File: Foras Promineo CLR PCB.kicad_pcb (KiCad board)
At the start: 2 copper layers, 40 x 40 mm, 21 parts, among them J1 Conn_01x10_Male

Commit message: FM DONE!
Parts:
- D3: footprint Foras_Promineo:1212_LED_Pol_End -> Foras_Promineo_Github_Local:1212_LED_Pol
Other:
- board text added: "FORAS PROMINEO LED RING - CLR REV: FLIGHT NB, CK 06/2022"
- board text removed: "CLR FORAS PROMINEO LED RING REV: FLIGHT NB, CK 4/2022 SN:"
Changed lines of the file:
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@@
   (setup
     (stackup
-      (layer "F.SilkS" (type "Top Silk Screen"))
+      (layer "F.SilkS" (type "Top Silk Screen") (color "Black"))
       (layer "F.Paste" (type "Top Solder Paste"))
-      (layer "F.Mask" (type "Top Solder Mask") (thickness 0.01))
+      (layer "F.Mask" (type "Top Solder Mask") (color "White") (thickness 0.01))
       (layer "F.Cu" (type "copper") (thickness 0.035))
       (layer "dielectric 1" (type "core") (thickness 1.51) (material "FR4") (epsilon_r 4.5) (loss_tangent 0.02))
       (layer "B.Cu" (type "copper") (thickness 0.035))
-      (layer "B.Mask" (type "Bottom Solder Mask") (thickness 0.01))
+      (layer "B.Mask" (type "Bottom Solder Mask") (color "White") (thickness 0.01))
       (layer "B.Paste" (type "Bottom Solder Paste"))
-      (layer "B.SilkS" (type "Bottom Silk Screen"))
+      (layer "B.SilkS" (type "Bottom Silk Screen") (color "Black"))
       (copper_finish "None")
       (dielectric_constraints no)
@@
     (grid_origin 80 88)
     (pcbplotparams
-      (layerselection 0x00010fc_ffffffff)
+      (layerselection 0x00210ff_ffffffff)
       (disableapertmacros false)
       (usegerberextensions true)
@@
       (drillshape 0)
       (scaleselection 1)
-      (outputdirectory "../../../Foras Promineo CLR PCB/")
+      (outputdirectory "Fab Files/")
     )
   )
@@
     )
   )
-  (footprint "Foras_Promineo:1212_LED_Pol_End" (layer "F.Cu")
+  (footprint "Foras_Promineo_Github_Local:1212_LED_Pol" (layer "F.Cu")
     (at 89.289 96.684 45)
     (property "Description" "LED Lighting series White - 2.75V 65mA 120° 1212 (3030 Metric)")
@@
     (property "Supplier Part Number" "1510-SPMWHD32AMH1XAH0S0CT-ND")
     (attr through_hole)
-    (fp_text reference "D3" (at -0.286378 2.706098 45) (layer "F.SilkS")
+    (fp_text reference "D3" (at 3.956262 -0.122329 45) (layer "F.SilkS")
       (effects (font (size 1 1) (thickness 0.15)))
     )
@@
       (effects (font (size 1 1) (thickness 0.15)))
     )
-    (fp_circle (center 1.25 2.5) (end 1.5 2.5) (layer "F.SilkS") (width 0.15) (fill solid))
-    (fp_line (start -1.3 -1.6) (end 1.3 -1.6) (layer "Eco1.User") (width 0.12))
-    (fp_line (start -1.3 1.6) (end -1.3 -1.6) (layer "Eco1.User") (width 0.12))
+    (fp_line (start 2.5 -1.75) (end 2.5 1.75) (layer "F.SilkS") (width 0.15))
     (fp_line (start 1.3 1.6) (end -1.3 1.6) (layer "Eco1.User") (width 0.12))
     (fp_line (start 1.3 -1.6) (end 1.3 1.6) (layer "Eco1.User") (width 0.12))
+    (fp_line (start -1.3 -1.6) (end 1.3 -1.6) (layer "Eco1.User") (width 0.12))
+    (fp_line (start -1.3 1.6) (end -1.3 -1.6) (layer "Eco1.User") (width 0.12))
     (pad "1" smd rect (at 1.025 0 45) (size 1.75 3.5) (layers "F.Cu" "F.Paste" "F.Mask")
       (net 12 "/LED_3") (pinfunction "K") (pintype "passive"))
@@
     (property "Supplier Part Number" "1510-SPMWHD32AMH1XAH0S0CT-ND")
     (attr through_hole)
-    (fp_text reference "D4" (at 1.640488 -3.112684 225) (layer "F.SilkS")
+    (fp_text reference "D4" (at 3.478965 0.140007 225) (layer "F.SilkS")
       (effects (font (size 1 1) (thickness 0.15)))
     )
@@
   (gr_line (start 98 60) (end 62 60) (layer "Edge.Cuts") (width 0.1))
   (gr_arc (start 98 60) (mid 99.414214 60.585786) (end 100 62) (layer "Edge.Cuts") (width 0.1))
-  (gr_text "CLR\nFORAS PROMINEO LED RING\nREV: FLIGHT\nNB, CK\n4/2022\nSN:" (at 79.9 63.5) (layer "F.SilkS")
+  (gr_text "FORAS PROMINEO LED RING - CLR\nREV: FLIGHT\nNB, CK\n06/2022" (at 79.8 63.2) (layer "F.SilkS")
     (effects (font (size 0.75 0.75) (thickness 0.15)))
   )

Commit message: FM
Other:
- board text added: "FORAS PROMINEO LED RING - CLR REV: FM NB, CK 09/2022"
- board text removed: "FORAS PROMINEO LED RING - CLR REV: FLIGHT NB, CK 06/2022"
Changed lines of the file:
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@@
       (drillshape 0)
       (scaleselection 1)
-      (outputdirectory "Fab Files/")
+      (outputdirectory "Fab Files/FM/")
     )
   )
@@
     )
   )
+  (gr_rect (start 91.380005 71.390002) (end 98.009989 98.349994) (layer "B.SilkS") (width 0.254) (fill none))
   (gr_circle (center 94.73 66.55) (end 96.73 66.55) (layer "Eco1.User") (width 0.2) (fill none))
   (gr_circle (center 65.27 66.55) (end 67.27 66.55) (layer "Eco1.User") (width 0.2) (fill none))
@@
   (gr_line (start 98 60) (end 62 60) (layer "Edge.Cuts") (width 0.1))
   (gr_arc (start 98 60) (mid 99.414214 60.585786) (end 100 62) (layer "Edge.Cuts") (width 0.1))
-  (gr_text "FORAS PROMINEO LED RING - CLR\nREV: FLIGHT\nNB, CK\n06/2022" (at 79.8 63.2) (layer "F.SilkS")
+  (gr_text "FORAS PROMINEO LED RING - CLR\nREV: FM\nNB, CK\n09/2022" (at 79.799993 63.200001) (layer "F.SilkS")
     (effects (font (size 0.75 0.75) (thickness 0.15)))
   )

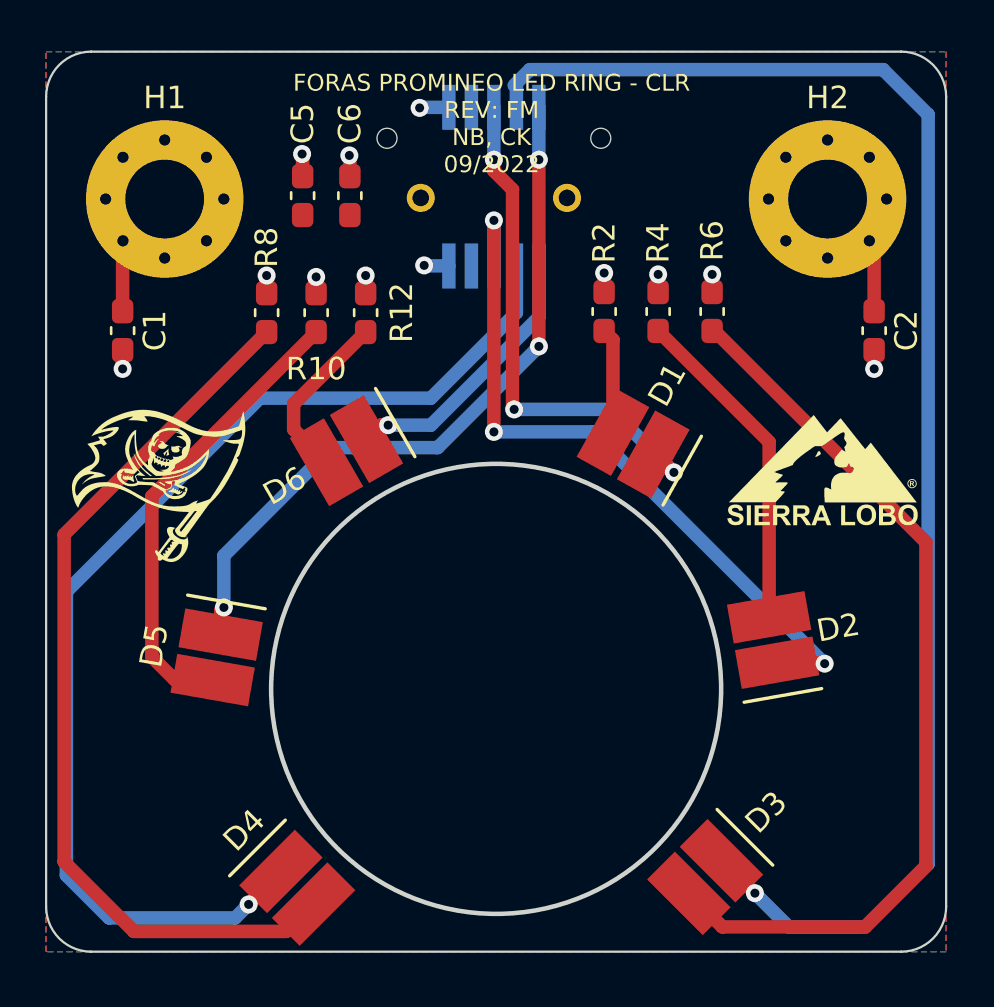
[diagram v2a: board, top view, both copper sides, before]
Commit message: moved mounting holes and added fiducials
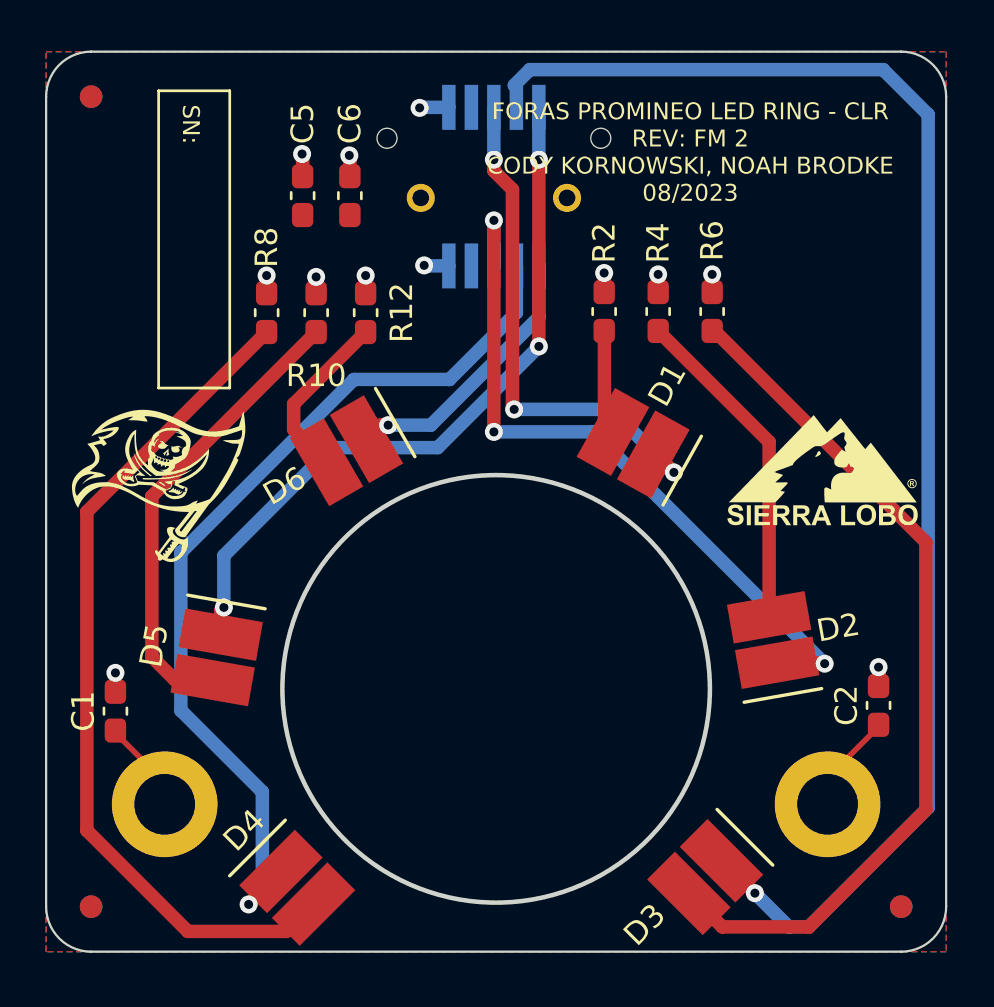
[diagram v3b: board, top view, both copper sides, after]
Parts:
- added REF**: Fiducial_1mm_Mask3mm, Fiducial:Fiducial_1mm_Mask3mm, F.Cu at (62.0, 62.0)
- added REF**: Fiducial_1mm_Mask3mm, Fiducial:Fiducial_1mm_Mask3mm, F.Cu at (98.0, 98.0)
- added REF**: Fiducial_1mm_Mask3mm, Fiducial:Fiducial_1mm_Mask3mm, F.Cu at (62.0, 98.0)
- added REF**: Fiducial_1mm_Mask3mm, Fiducial:Fiducial_1mm_Mask3mm, B.Cu at (62.0, 98.0)
- added REF**: Fiducial_1mm_Mask3mm, Fiducial:Fiducial_1mm_Mask3mm, B.Cu at (98.0, 98.0)
- added REF**: Fiducial_1mm_Mask3mm, Fiducial:Fiducial_1mm_Mask3mm, B.Cu at (62.0, 62.0)
- H1, H2: footprint MountingHole:MountingHole_3.5mm_Pad_Via -> MountingHole:MountingHole_2.7mm_M2.5_DIN965_Pad
- moved H1 26.9 mm to (65.3, 93.4)
- moved H2 26.9 mm to (94.7, 93.4)
- moved C1 16.9 mm to (63.1, 89.3), turned to 90 degrees
- moved C2 16.7 mm to (97.0, 89.1), turned to 90 degrees
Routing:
- net /LED_4: track 51.0 -> 40.9 mm
- net Net-(D4-A): track 40.1 -> 37.9 mm
- net Net-(C1-Pad1): track 5.85 -> 4.18 mm
- net Net-(D3-A): track 40.1 -> 38.6 mm
- net /LED_3: track 64.4 -> 62.9 mm
- net Net-(C2-Pad1): track 5.93 -> 4.47 mm
- net GND: track 3.67 -> 2.74 mm
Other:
- outline, holes or cut-outs redrawn
- board text added: "FORAS PROMINEO LED RING - CLR REV: FM 2 CODY KORNOWSKI, NOAH BRODKE 08/2023"
- board text added: "SN:"
- board text removed: "FORAS PROMINEO LED RING - CLR REV: FM NB, CK 09/2022"

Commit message: updates
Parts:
- moved REF** 35.0 mm to (96.2, 63.0) (x2)
- moved REF** 1.02 mm to (62.2, 63.0) (x2)
- moved REF** 0.20 mm to (62.2, 98.0) (x2)
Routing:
- net /LED_3: track 62.9 -> 57.0 mm
- net Net-(D3-A): track 38.6 -> 39.4 mm
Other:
- board size 40 x 40 mm -> 39.8 x 39.8 mm
- board text added: "FORAS PROMINEO - CLR REV: FM 2 CK, NB 08/2023"
- board text removed: "FORAS PROMINEO LED RING - CLR REV: FM 2 CODY KORNOWSKI, NOAH BRODKE 08/2023"

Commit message: LED RING
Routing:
- net /LED_3: track 57.0 -> 55.0 mm
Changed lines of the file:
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@@
   )
   (footprint "MountingHole:MountingHole_2.7mm_M2.5_DIN965_Pad" (layer "F.Cu")
-    (at 65.27 93.44983)
+    (at 65.27 93.45)
     (descr "Mounting Hole 2.7mm, M2.5, DIN965")
     (tags "mounting hole 2.7mm m2.5 din965")
@@
   )
   (footprint "MountingHole:MountingHole_2.7mm_M2.5_DIN965_Pad" (layer "F.Cu")
-    (at 94.73 93.44983)
+    (at 94.73 93.45)
     (descr "Mounting Hole 2.7mm, M2.5, DIN965")
     (tags "mounting hole 2.7mm m2.5 din965")
@@
   (gr_line (start 60.2 62.2) (end 60.2 98)
     (stroke (width 0.1) (type solid)) (layer "Edge.Cuts"))
-  (gr_circle (center 80 88.31983) (end 89.5 88.31983)
+  (gr_circle (center 80 88.32) (end 89.5 88.32)
     (stroke (width 0.2) (type solid)) (fill none) (layer "Edge.Cuts"))
   (gr_arc (start 60.2 62.2) (mid 60.785786 60.785786) (end 62.2 60.2)
@@
   )
   (dimension (type orthogonal) (layer "Eco1.User")
+    (pts (xy 94.729293 93.450537) (xy 100 94))
+    (height 10.749463)
+    (orientation 0)
+    (gr_text "5.2707 mm" (at 97.364647 103.05) (layer "Eco1.User")
+      (effects (font (size 1 1) (thickness 0.15)))
+    )
+    (format (prefix "") (suffix "") (units 3) (units_format 1) (precision 4))
+    (style (thickness 0.1) (arrow_length 1.27) (text_position_mode 0) (extension_height 0.58642) (extension_offset 0.5) keep_text_aligned)
+  )
+  (dimension (type orthogonal) (layer "Eco1.User")
     (pts (xy 60.2 100) (xy 65.27 93.44983))
     (height 7.4)
@@
   (segment (start 95.3 98.9) (end 90.055432 98.9) (width 0.6) (layer "F.Cu") (net 5))
   (segment (start 99.1 81.8) (end 99.1 95.1) (width 0.6) (layer "F.Cu") (net 5))
+  (segment (start 61.81 80.4525) (end 61.81 94.41) (width 0.6) (layer "F.Cu") (net 6))
+  (segment (start 61.81 94.41) (end 64.8 97.4) (width 0.6) (layer "F.Cu") (net 6))
+  (segment (start 66.8 97.4) (end 68.5 99.1) (width 0.6) (layer "F.Cu") (net 6))
   (segment (start 69.8 72.4625) (end 61.81 80.4525) (width 0.6) (layer "F.Cu") (net 6))
-  (segment (start 61.81 80.4525) (end 61.81 94.61) (width 0.6) (layer "F.Cu") (net 6))
-  (segment (start 66.3 99.1) (end 70.669568 99.1) (width 0.6) (layer "F.Cu") (net 6))
-  (segment (start 61.81 94.61) (end 66.3 99.1) (width 0.6) (layer "F.Cu") (net 6))
+  (segment (start 64.8 97.4) (end 66.8 97.4) (width 0.6) (layer "F.Cu") (net 6))
+  (segment (start 68.5 99.1) (end 70.669568 99.1) (width 0.6) (layer "F.Cu") (net 6))
   (segment (start 70.669568 99.1) (end 71.885784 97.883784) (width 0.6) (layer "F.Cu") (net 6))
   (segment (start 65.729428 87.929428) (end 64.7 86.9) (width 0.6) (layer "F.Cu") (net 7))
@@
   (segment (start 90.059216 95.959216) (end 91.5 97.4) (width 0.6) (layer "F.Cu") (net 12))
   (via (at 91.5 97.4) (size 0.8) (drill 0.4) (layers "F.Cu" "B.Cu") (net 12))
-  (segment (start 82.6 68) (end 92.8 68) (width 0.6) (layer "B.Cu") (net 12))
-  (segment (start 97.2 86) (end 97.2 72.4) (width 0.6) (layer "B.Cu") (net 12))
+  (segment (start 94.9 98.9) (end 93 98.9) (width 0.6) (layer "B.Cu") (net 12))
+  (segment (start 97.2 75.8) (end 97.2 86) (width 0.6) (layer "B.Cu") (net 12))
   (segment (start 80.9 62.475) (end 80.9 66.3) (width 0.6) (layer "B.Cu") (net 12))
-  (segment (start 94.9 98.9) (end 98.2 95.6) (width 0.6) (layer "B.Cu") (net 12))
-  (segment (start 98.2 95.6) (end 98.2 87) (width 0.6) (layer "B.Cu") (net 12))
-  (segment (start 91.5 97.4) (end 93 98.9) (width 0.6) (layer "B.Cu") (net 12))
-  (segment (start 93 98.9) (end 94.9 98.9) (width 0.6) (layer "B.Cu") (net 12))
-  (segment (start 80.9 66.3) (end 82.6 68) (width 0.6) (layer "B.Cu") (net 12))
-  (segment (start 98.2 87) (end 97.2 86) (width 0.6) (layer "B.Cu") (net 12))
-  (segment (start 92.8 68) (end 97.2 72.4) (width 0.6) (layer "B.Cu") (net 12))
+  (segment (start 98.2 95.6) (end 94.9 98.9) (width 0.6) (layer "B.Cu") (net 12))
+  (segment (start 98.2 87) (end 98.2 95.6) (width 0.6) (layer "B.Cu") (net 12))
+  (segment (start 97.2 86) (end 98.2 87) (width 0.6) (layer "B.Cu") (net 12))
+  (segment (start 90 68.6) (end 97.2 75.8) (width 0.6) (layer "B.Cu") (net 12))
+  (segment (start 93 98.9) (end 91.5 97.4) (width 0.6) (layer "B.Cu") (net 12))
+  (segment (start 80.9 66.3) (end 83.2 68.6) (width 0.6) (layer "B.Cu") (net 12))
+  (segment (start 83.2 68.6) (end 90 68.6) (width 0.6) (layer "B.Cu") (net 12))
   (segment (start 79.9 76.9) (end 79.9 67.5) (width 0.6) (layer "F.Cu") (net 13))
   (segment (start 94.558428 87.158428) (end 94.6 87.2) (width 0.6) (layer "F.Cu") (net 13))

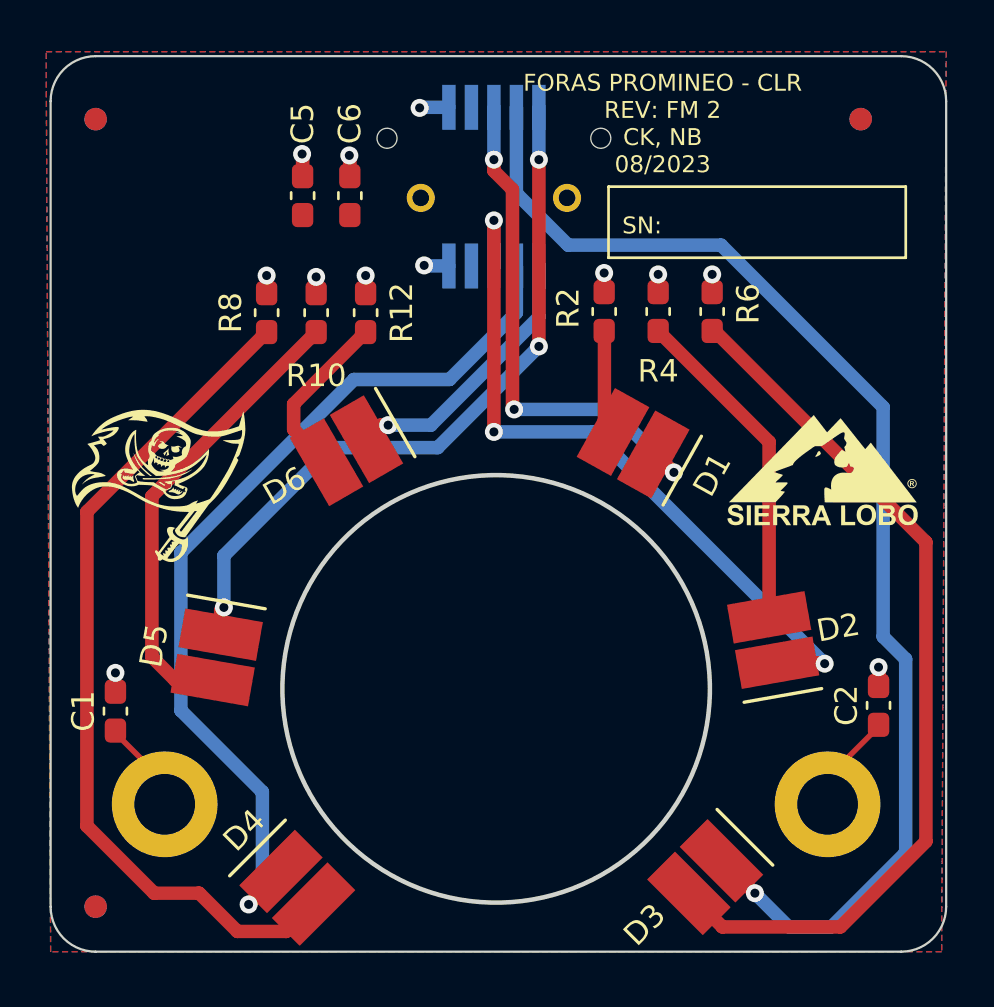
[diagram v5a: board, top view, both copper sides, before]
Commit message: Fixed LED board shape again...
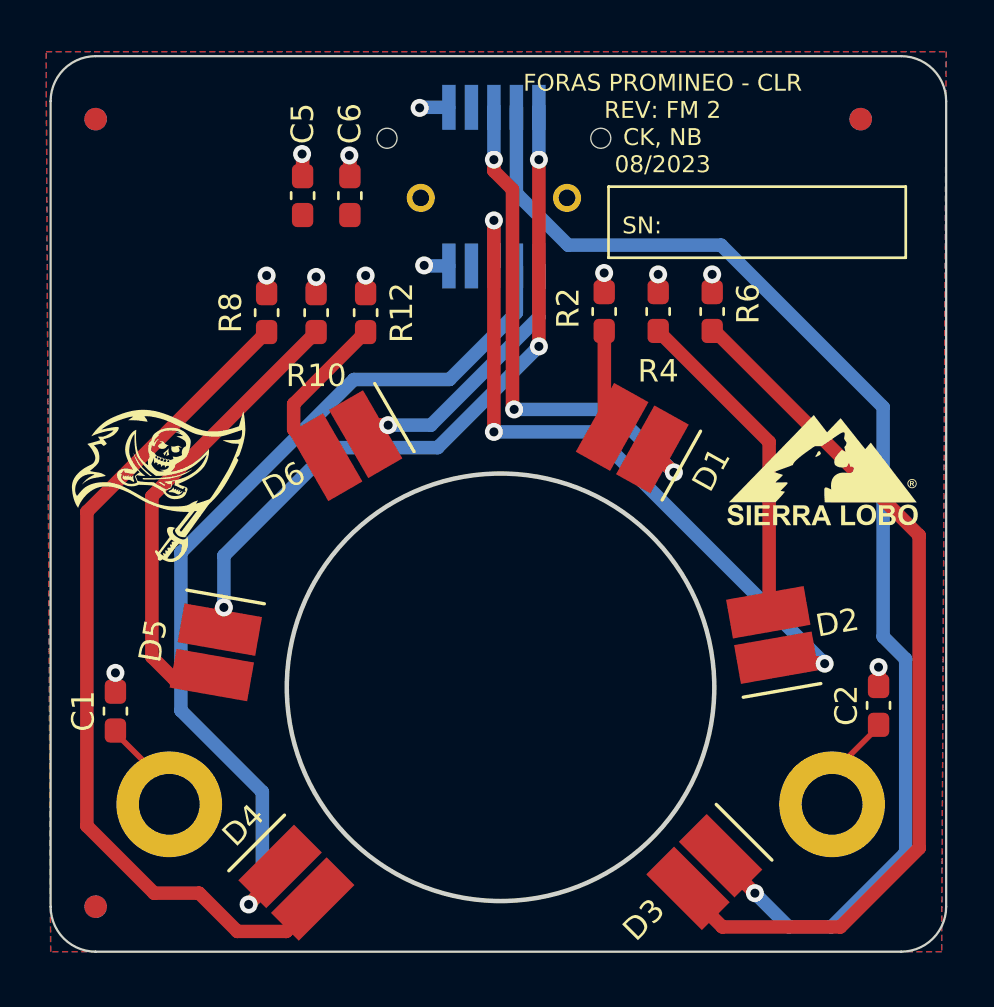
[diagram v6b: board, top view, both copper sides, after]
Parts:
- moved D1 0.23 mm to (86.0, 77.2)
- moved D2 0.23 mm to (92.3, 85.9)
- moved D3 0.23 mm to (89.3, 96.5)
- moved D4 0.23 mm to (71.1, 96.9)
- moved D5 0.23 mm to (67.5, 86.7)
- moved D6 0.23 mm to (73.3, 77.5)
- moved H1 0.20 mm to (65.5, 93.5)
- moved H2 0.20 mm to (94.9, 93.5)
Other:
- outline, holes or cut-outs redrawn

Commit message: FM2 fab files
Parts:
- moved D4 0.43 mm to (71.4, 96.6)
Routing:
- net /LED_4: track 40.9 -> 37.6 mm
